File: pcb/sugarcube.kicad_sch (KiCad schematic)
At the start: 0 parts

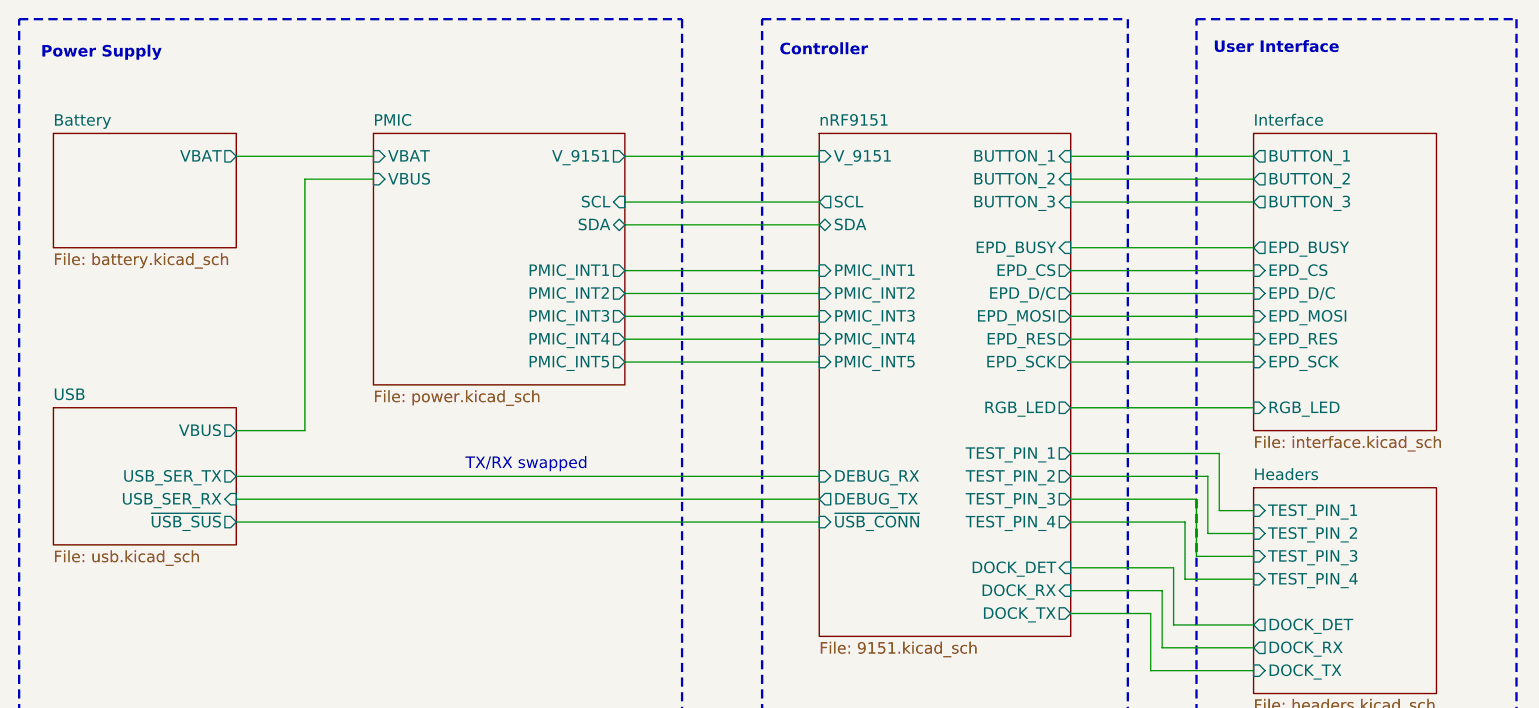
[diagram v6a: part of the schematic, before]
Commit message: Fix display sch
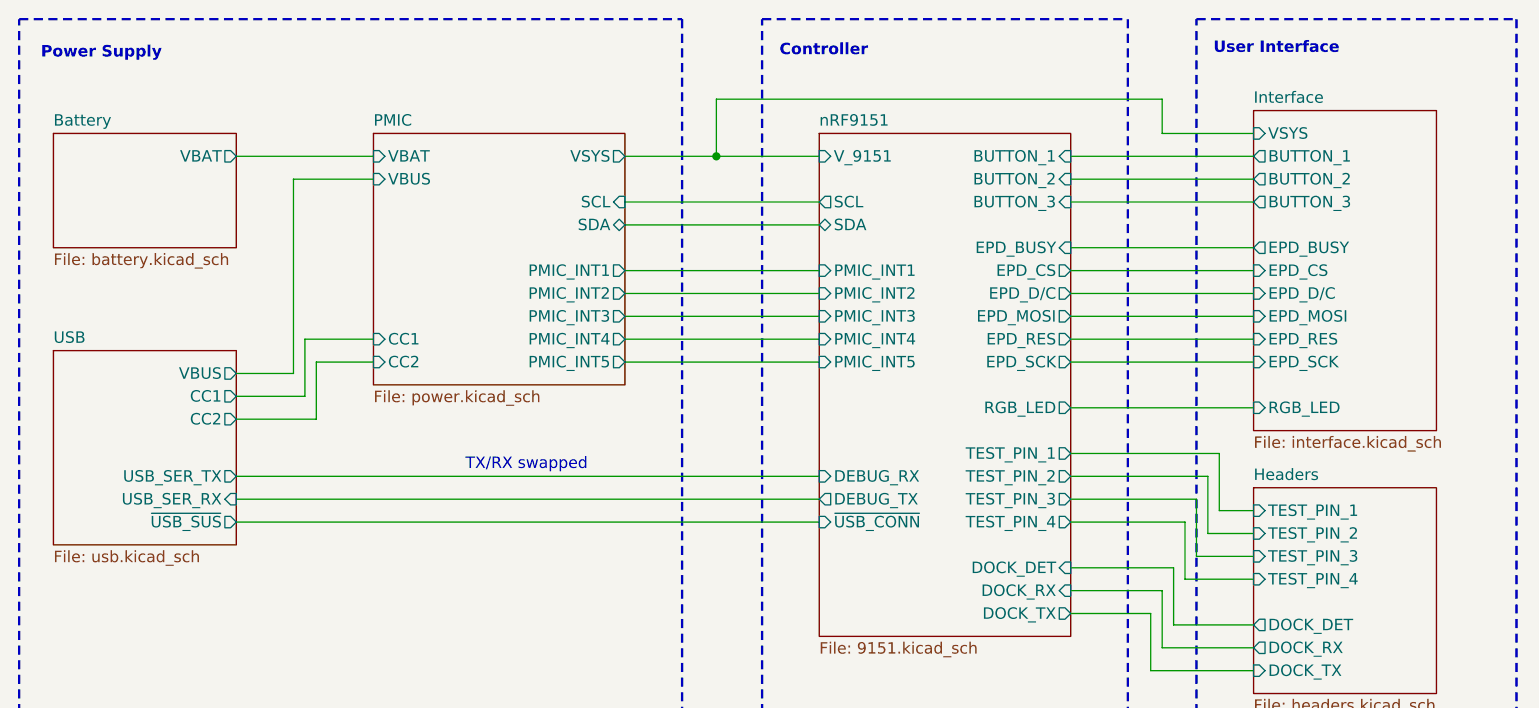
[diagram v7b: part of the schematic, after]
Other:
- sheet Interface ports: added VSYS; removed none
- sheet PMIC ports: added CC1, CC2, VSYS; removed V_9151
- sheet USB ports: added CC1, CC2; removed none
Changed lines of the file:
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@@
 		)
+	)
+	(junction
+		(at 143.51 72.39)
+		(diameter 0)
+		(color 0 0 0 0)
 	)
 	(wire
@@
 	(wire
 		(pts
-			(xy 97.79 74.93) (xy 105.41 74.93)
+			(xy 90.17 96.52) (xy 96.52 96.52)
+		)
+		(stroke
+			(width 0)
+			(type default)
+		)
+	)
+	(wire
+		(pts
+			(xy 97.79 99.06) (xy 97.79 92.71)
+		)
+		(stroke
+			(width 0)
+			(type default)
+		)
+	)
+	(wire
+		(pts
+			(xy 99.06 101.6) (xy 99.06 95.25)
 		)
 		(stroke
@@
 	(wire
 		(pts
+			(xy 143.51 72.39) (xy 154.94 72.39)
+		)
+		(stroke
+			(width 0)
+			(type default)
+		)
+	)
+	(wire
+		(pts
 			(xy 133.35 80.01) (xy 154.94 80.01)
 		)
@@
 	(wire
 		(pts
+			(xy 99.06 95.25) (xy 105.41 95.25)
+		)
+		(stroke
+			(width 0)
+			(type default)
+		)
+	)
+	(wire
+		(pts
 			(xy 196.85 116.84) (xy 203.2 116.84)
 		)
@@
 	(wire
 		(pts
+			(xy 90.17 99.06) (xy 97.79 99.06)
+		)
+		(stroke
+			(width 0)
+			(type default)
+		)
+	)
+	(wire
+		(pts
 			(xy 133.35 95.25) (xy 154.94 95.25)
 		)
@@
 	(wire
 		(pts
+			(xy 193.04 66.04) (xy 193.04 69.85)
+		)
+		(stroke
+			(width 0)
+			(type default)
+		)
+	)
+	(wire
+		(pts
 			(xy 199.39 111.76) (xy 203.2 111.76)
 		)
@@
 	(wire
 		(pts
+			(xy 193.04 69.85) (xy 203.2 69.85)
+		)
+		(stroke
+			(width 0)
+			(type default)
+		)
+	)
+	(wire
+		(pts
 			(xy 182.88 87.63) (xy 203.2 87.63)
 		)
@@
 	(wire
 		(pts
+			(xy 143.51 66.04) (xy 193.04 66.04)
+		)
+		(stroke
+			(width 0)
+			(type default)
+		)
+	)
+	(wire
+		(pts
 			(xy 194.31 124.46) (xy 194.31 118.11)
 		)
@@
 	(wire
 		(pts
-			(xy 90.17 102.87) (xy 97.79 102.87)
+			(xy 90.17 101.6) (xy 99.06 101.6)
+		)
+		(stroke
+			(width 0)
+			(type default)
+		)
+	)
+	(wire
+		(pts
+			(xy 96.52 74.93) (xy 105.41 74.93)
 		)
 		(stroke
@@
 	(wire
 		(pts
-			(xy 97.79 102.87) (xy 97.79 74.93)
-		)
-		(stroke
-			(width 0)
-			(type default)
-		)
-	)
-	(wire
-		(pts
 			(xy 182.88 95.25) (xy 203.2 95.25)
 		)
@@
 	(wire
 		(pts
-			(xy 133.35 72.39) (xy 154.94 72.39)
+			(xy 133.35 72.39) (xy 143.51 72.39)
 		)
 		(stroke
@@
 	(wire
 		(pts
+			(xy 97.79 92.71) (xy 105.41 92.71)
+		)
+		(stroke
+			(width 0)
+			(type default)
+		)
+	)
+	(wire
+		(pts
 			(xy 195.58 119.38) (xy 195.58 113.03)
 		)
@@
 	(wire
 		(pts
+			(xy 143.51 72.39) (xy 143.51 66.04)
+		)
+		(stroke
+			(width 0)
+			(type default)
+		)
+	)
+	(wire
+		(pts
 			(xy 90.17 110.49) (xy 154.94 110.49)
 		)
@@
 		(pts
 			(xy 193.04 127) (xy 193.04 120.65)
+		)
+		(stroke
+			(width 0)
+			(type default)
+		)
+	)
+	(wire
+		(pts
+			(xy 96.52 96.52) (xy 96.52 74.93)
 		)
 		(stroke
@@
 			)
 		)
-		(pin "V_9151" output
-			(at 133.35 72.39 0)
-			(effects
-				(font
-					(size 1.27 1.27)
-				)
-				(justify right)
-			)
-		)
 		(pin "PMIC_INT1" output
 			(at 133.35 85.09 0)
@@
 		(pin "VBUS" input
 			(at 105.41 74.93 180)
+			(effects
+				(font
+					(size 1.27 1.27)
+				)
+				(justify left)
+			)
+		)
+		(pin "VSYS" output
+			(at 133.35 72.39 0)
+			(effects
+				(font
+					(size 1.27 1.27)
+				)
+				(justify right)
+			)
+		)
+		(pin "CC1" input
+			(at 105.41 92.71 180)
+			(effects
+				(font
+					(size 1.27 1.27)
+				)
+				(justify left)
+			)
+		)
+		(pin "CC2" input
+			(at 105.41 95.25 180)
 			(effects
 				(font
@@
 	)
 	(sheet
-		(at 69.85 100.33)
-		(size 20.32 15.24)
+		(at 69.85 93.98)
+		(size 20.32 21.59)
 		(exclude_from_sim no)
 		(in_bom yes)
@@
 		)
 		(property "Sheetname" "USB"
-			(at 69.85 99.6184 0)
+			(at 69.85 93.2684 0)
 			(effects
 				(font
@@
 		)
 		(pin "VBUS" output
-			(at 90.17 102.87 0)
+			(at 90.17 96.52 0)
+			(effects
+				(font
+					(size 1.27 1.27)
+				)
+				(justify right)
+			)
+		)
+		(pin "CC1" output
+			(at 90.17 99.06 0)
+			(effects
+				(font
+					(size 1.27 1.27)
+				)
+				(justify right)
+			)
+		)
+		(pin "CC2" output
+			(at 90.17 101.6 0)
 			(effects
 				(font
@@
 	)
 	(sheet
-		(at 203.2 69.85)
-		(size 20.32 33.02)
+		(at 203.2 67.31)
+		(size 20.32 35.56)
 		(exclude_from_sim no)
 		(in_bom yes)
@@
 		)
 		(property "Sheetname" "Interface"
-			(at 203.2 69.1384 0)
+			(at 203.2 66.5984 0)
 			(effects
 				(font
@@
 			(effects
 				(font
+					(size 1.27 1.27)
+				)
+				(justify left)
+			)
+		)
+		(pin "VSYS" input
+			(at 203.2 69.85 180)
+			(effects
+				(font

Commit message: clean up
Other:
- sheet nRF9151 renamed Modem
- note added: "Controller/RF"
- note removed: "Controller"
